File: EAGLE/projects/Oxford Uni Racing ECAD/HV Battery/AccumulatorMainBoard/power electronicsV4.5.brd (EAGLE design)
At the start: 167.6 x 103.8 mm, 94 parts, among them IC1 4043D, IC2 SE555D, IC9 4011D, K2 T9AS5D12-12=T9A, K3 T9AS1D12-48=T9A, K6 T9AS1D12-48=T9A, K7 T9AS1D12-48=T9A, Q1 BSS138, Q2 BSS138, Q3 BSS138, Q4 BSS138

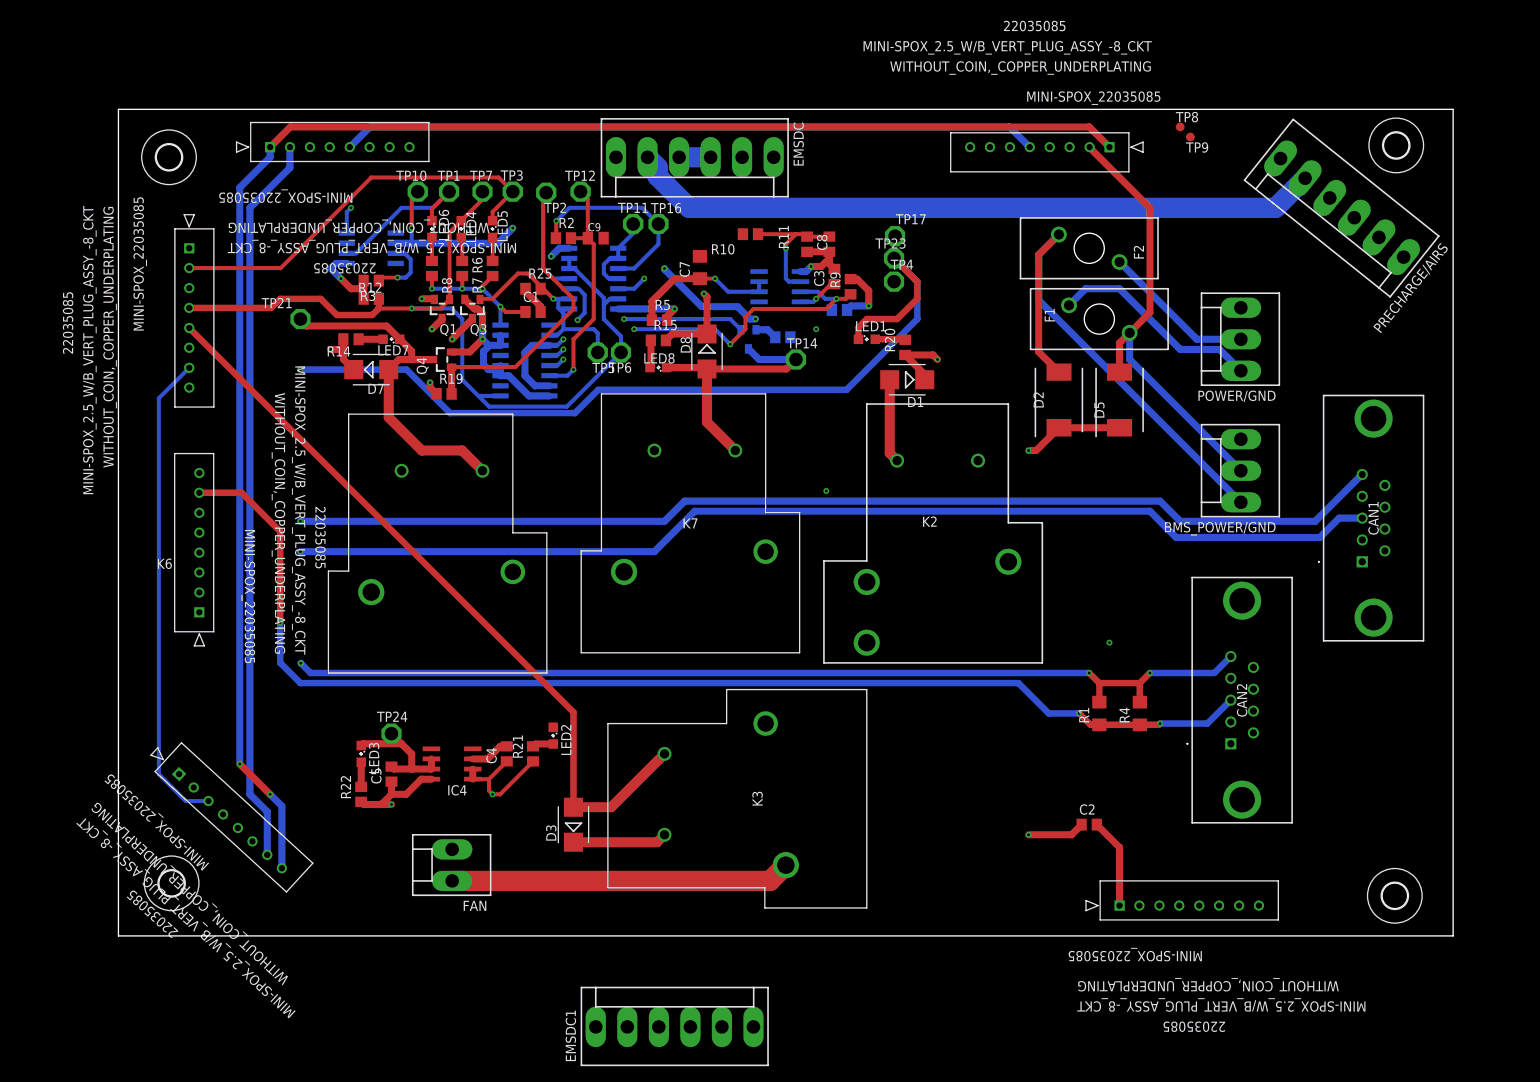
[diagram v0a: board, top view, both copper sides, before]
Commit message: Mainboard V4.5
New board layout, 2 layer design. removes circuits for fan and pre-charge.
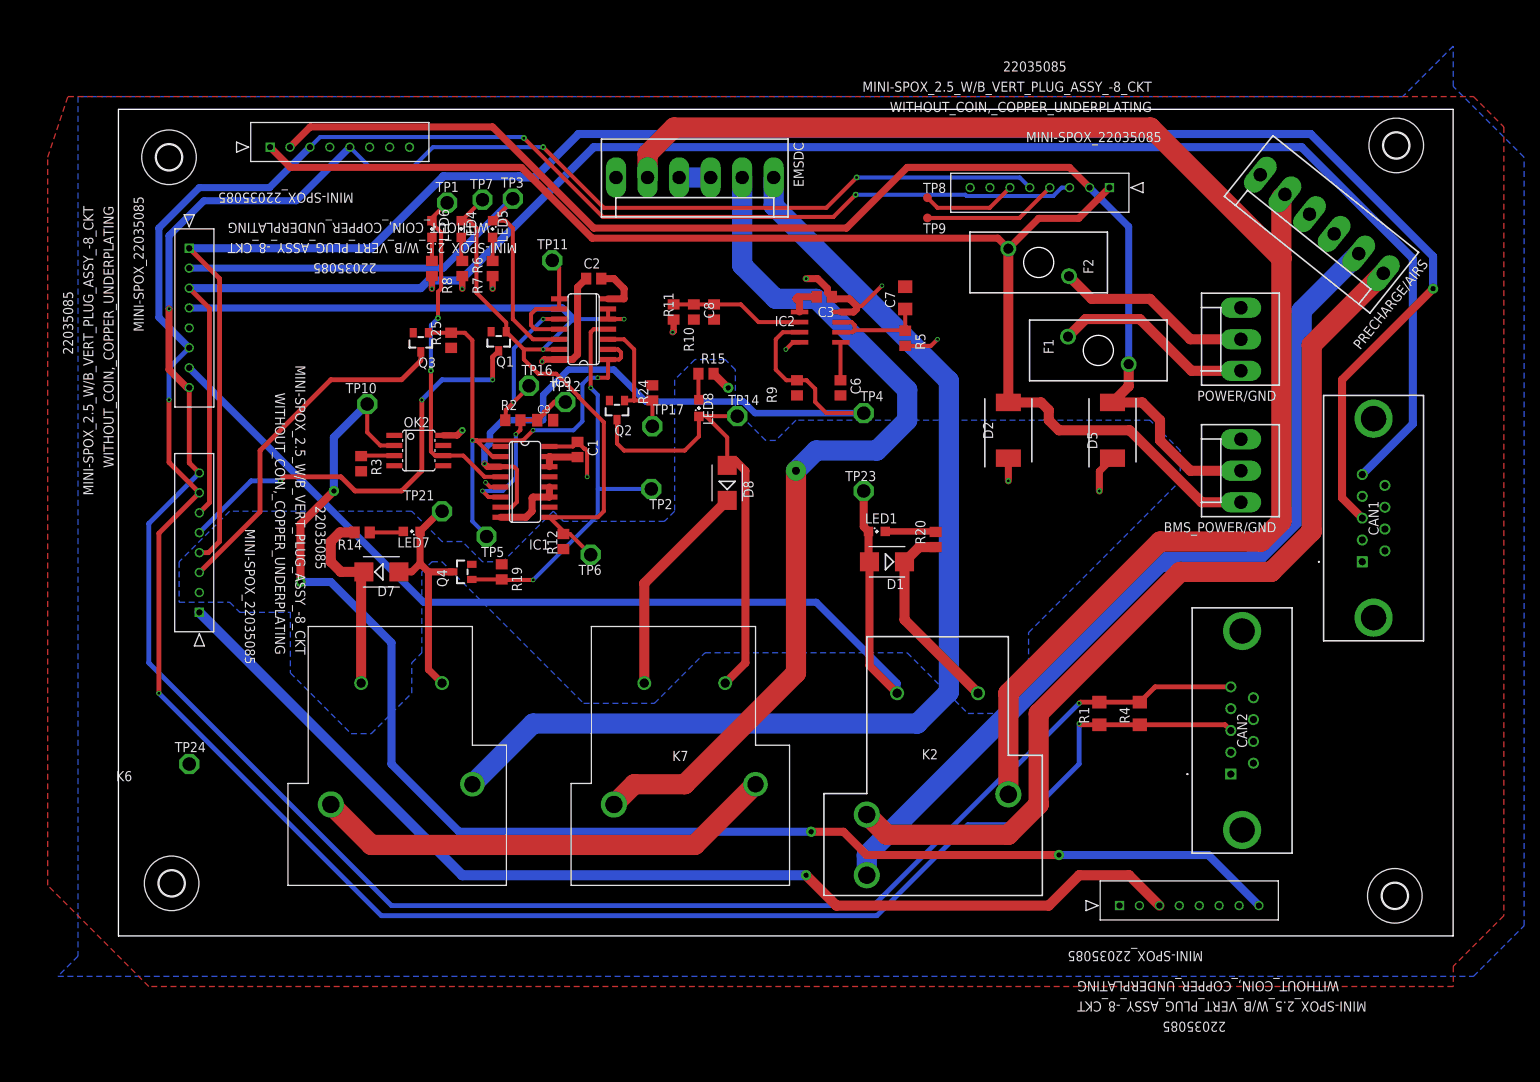
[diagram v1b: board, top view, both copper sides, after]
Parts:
- removed C4: 3.3uF, rcl:C0805
- removed C5: 1uF, rcl:C0805
- removed D3: ES2D, diode:SMB
- removed EMSDC1: (no value), con-molex:KK-156-6
- removed FAN: (no value), con-molex:KK-156-2
- removed IC4: (no value), linear-technology:SOIC8
- removed K3: T9AS1D12-48=T9A, SamacSys_Parts:T9AS1D1248T9A
- removed LED2, LED3: (no value), led:SML0805
- removed PRECHARGE: MINI-SPOX_22035085, Mini-spox_22035085:CON_22035085_MOL
- removed R21: 330, rcl:R0805
- removed R22: 1.2K, rcl:R0805
- moved C2 92.6 mm to (59.7, 82.5)
- moved TP2 39.5 mm to (66.9, 56.1)
- moved R12 38.9 mm to (55.9, 49.5), turned to 90 degrees
- moved TP17 38.7 mm to (67.1, 64.0)
- moved TP9 34.5 mm to (101.6, 90.2)
- moved TP8 33.0 mm to (101.6, 92.7)
- moved R5 30.9 mm to (98.8, 75.1), turned to 270 degrees
- moved TP21 30.0 mm to (40.6, 53.3)
- moved TP23 29.5 mm to (93.6, 55.9)
- moved K7 29.2 mm to (66.0, 31.8)
- moved K2 29.2 mm to (102.9, 30.5)
- moved TP10 27.4 mm to (31.2, 66.8)
- moved K6 27.1 mm to (30.5, 31.8)
- moved TP5 27.0 mm to (46.2, 50.2)
- moved Q4 26.8 mm to (43.2, 45.7)
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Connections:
- removed net FAN+: FAN.1, K3.4
- removed net FAN_ENABLE: BMS_I/O.5, D3.A, K3.2
- removed net N$23: LED2.A, R21.2
- removed net N$24: LED3.A, R22.2
- removed net PRECHARGE_EMSDC1: K6.3, PRECHARGE.1
- net +12V: no longer C5.1, D3.C, IC4.8, K3.1, K3.3, PRECHARGE.5, R22.1
- net +3V3: no longer C4.1, IC4.1, IC4.2, PRECHARGE.6, R21.1
- net CHARGE_POWER: no longer PRECHARGE.7
- net GND: no longer C4.2, C5.2, FAN.2, IC4.3, IC4.6, IC4.7, LED2.C, LED3.C, PRECHARGE.4
- net PRECHARGE_EMSDC2: now also K6.3; no longer PRECHARGE.2
- net PRECHARGE_SELECT: no longer PRECHARGE.3
- net READY_POWER: no longer PRECHARGE.8
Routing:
- net READY_POWER: track 280.0 -> 168.3 mm, vias 2 -> 0
- net FAN_ENABLE: track 94.4 -> 0.00 mm
- net CHARGE_POWER: track 250.5 -> 162.0 mm
- net GND: track 101.1 -> 25.5 mm, vias 8 -> 0
- net +3V3: track 128.3 -> 56.7 mm, vias 10 -> 12
- net PRECHARGE_SELECT: track 195.0 -> 133.7 mm, vias 1 -> 0
- net N$14: track 58.2 -> 113.7 mm, vias 0 -> 1
- net CAN1_H: track 193.5 -> 248.8 mm
- net PRECHARGE_EMSDC1: track 52.4 -> 0.00 mm
- net CAN2_H: track 302.4 -> 349.2 mm, vias 3 -> 5
- net CAN2_L: track 294.4 -> 338.0 mm, vias 3 -> 4
- net CAN1_L: track 182.9 -> 226.4 mm, vias 1 -> 0
- net FAN+: track 42.7 -> 0.00 mm
- net N$9: track 28.4 -> 65.2 mm, vias 1 -> 3
- net STARTUP_RESET: track 57.8 -> 90.7 mm, vias 4 -> 1
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- added copper zone on layer 16, net +12V
- added copper zone on layer 16, net +3V3
- added copper zone on layer 1, net GND
